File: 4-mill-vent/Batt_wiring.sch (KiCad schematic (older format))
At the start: 7 parts

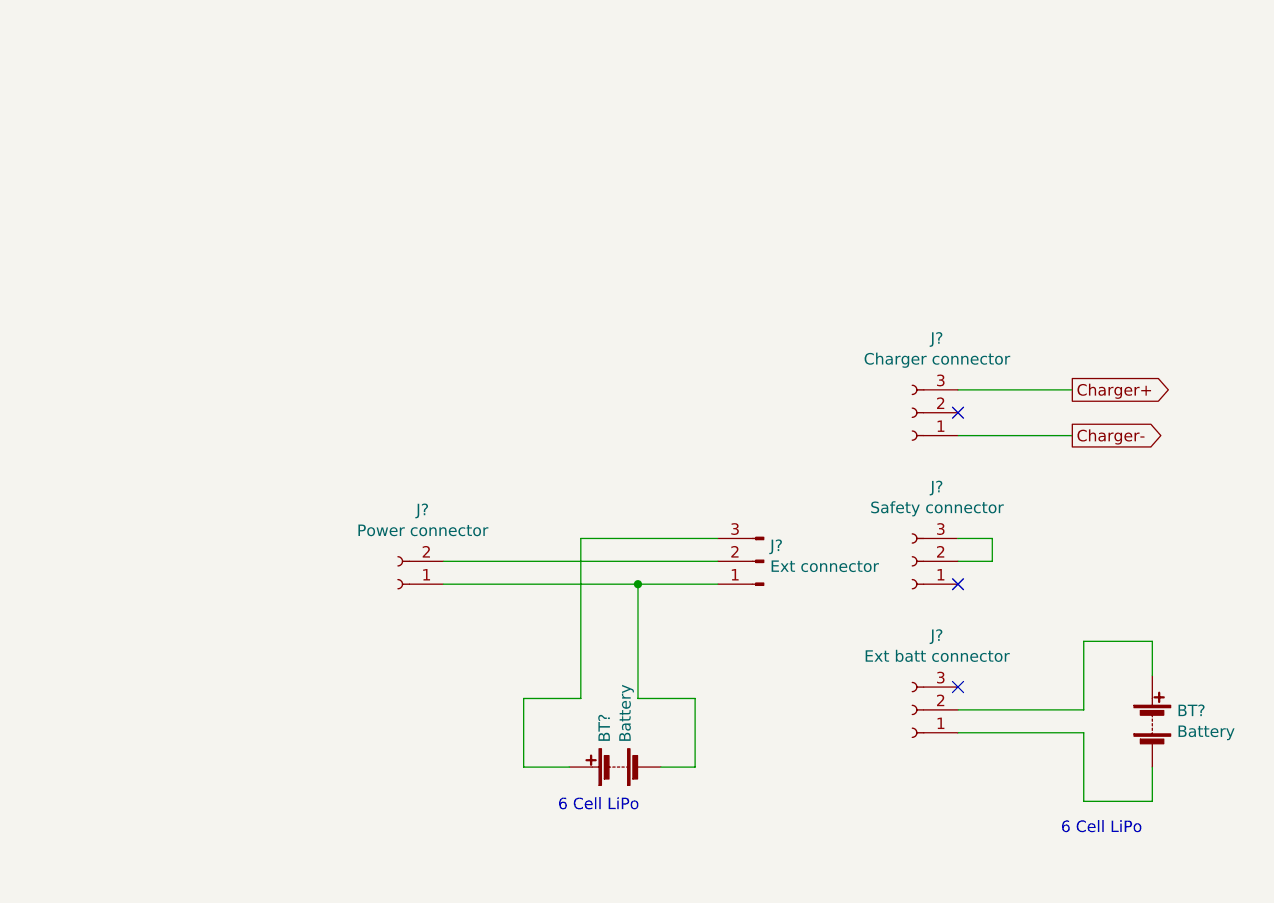
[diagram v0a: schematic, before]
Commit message: Added more to design
Had to add a transitor for allow the micro to power down the unit.
The reason is Q6's base can be as high as 16v when the on button is pressed.
This micro does not have open collector outputs and that would blow the chip.
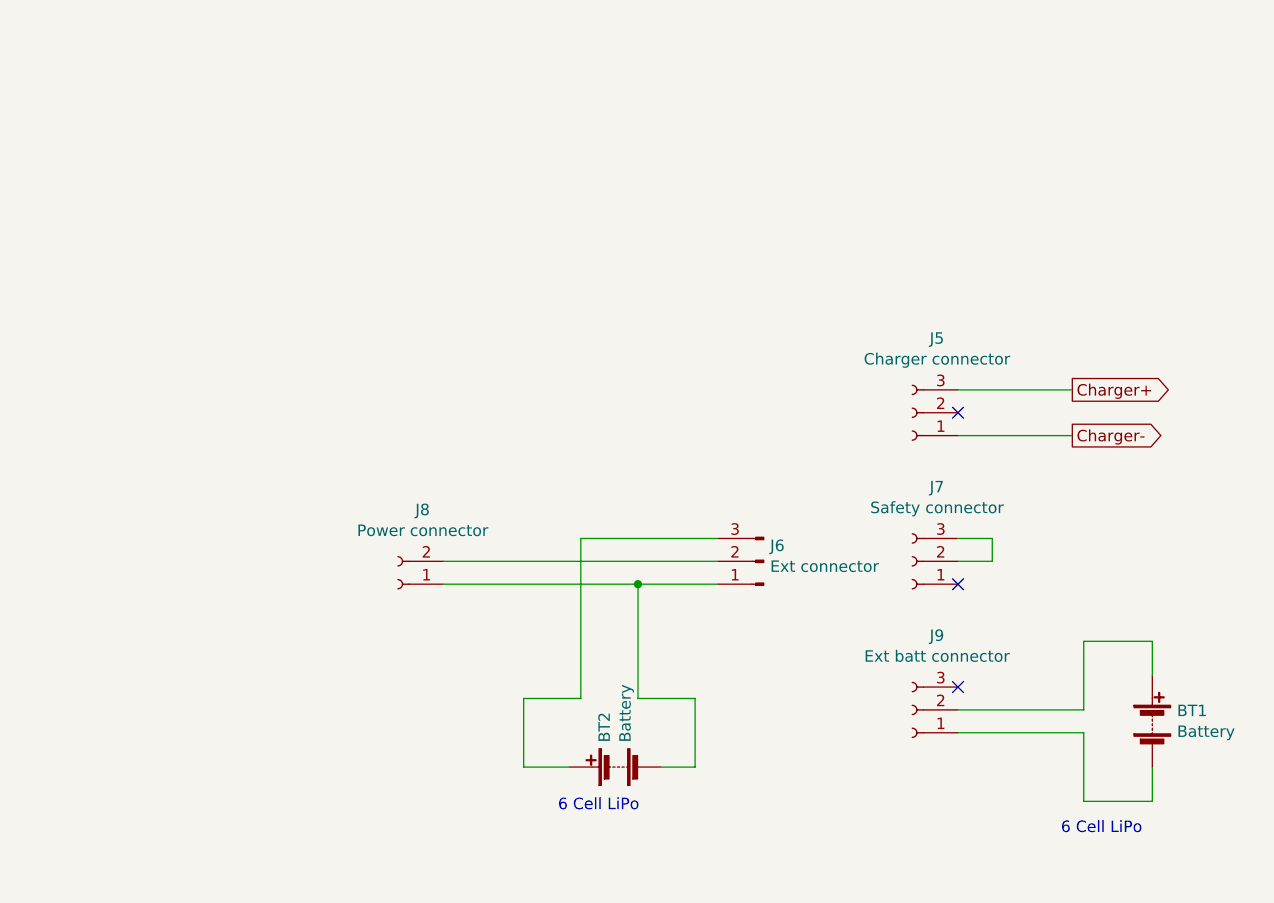
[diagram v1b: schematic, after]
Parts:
- gave numbers to parts that had none: 7
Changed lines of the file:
@@
 P 6250 3650
 AR Path="/5F8927BE" Ref="J?"  Part="1"
-AR Path="/5F88BDF3/5F8927BE" Ref="J?"  Part="1"
-F 0 "J?" H 6142 3325 50  0000 C CNN
+AR Path="/5F88BDF3/5F8927BE" Ref="J7"  Part="1"
+F 0 "J7" H 6142 3325 50  0000 C CNN
 F 1 "Safety connector" H 6142 3416 50  0000 C CNN
 F 2 "" H 6250 3650 50  0001 C CNN
@@
 P 6250 4300
 AR Path="/5F8927C4" Ref="J?"  Part="1"
-AR Path="/5F88BDF3/5F8927C4" Ref="J?"  Part="1"
-F 0 "J?" H 6142 3975 50  0000 C CNN
+AR Path="/5F88BDF3/5F8927C4" Ref="J9"  Part="1"
+F 0 "J9" H 6142 3975 50  0000 C CNN
 F 1 "Ext batt connector" H 6142 4066 50  0000 C CNN
 F 2 "" H 6250 4300 50  0001 C CNN
@@
 P 6250 3000
 AR Path="/5F8927CA" Ref="J?"  Part="1"
-AR Path="/5F88BDF3/5F8927CA" Ref="J?"  Part="1"
-F 0 "J?" H 6142 2675 50  0000 C CNN
+AR Path="/5F88BDF3/5F8927CA" Ref="J5"  Part="1"
+F 0 "J5" H 6142 2675 50  0000 C CNN
 F 1 "Charger connector" H 6142 2766 50  0000 C CNN
 F 2 "" H 6250 3000 50  0001 C CNN
@@
 P 5600 3650
 AR Path="/5F8927D0" Ref="J?"  Part="1"
-AR Path="/5F88BDF3/5F8927D0" Ref="J?"  Part="1"
-F 0 "J?" H 5572 3582 50  0000 R CNN
+AR Path="/5F88BDF3/5F8927D0" Ref="J6"  Part="1"
+F 0 "J6" H 5572 3582 50  0000 R CNN
 F 1 "Ext connector" H 5572 3673 50  0000 R CNN
 F 2 "" H 5600 3650 50  0001 C CNN
@@
 P 7300 4350
 AR Path="/5F8927DE" Ref="BT?"  Part="1"
-AR Path="/5F88BDF3/5F8927DE" Ref="BT?"  Part="1"
-F 0 "BT?" H 7408 4396 50  0000 L CNN
+AR Path="/5F88BDF3/5F8927DE" Ref="BT1"  Part="1"
+F 0 "BT1" H 7408 4396 50  0000 L CNN
 F 1 "Battery" H 7408 4305 50  0000 L CNN
 F 2 "" V 7300 4410 50  0001 C CNN
@@
 P 4950 4550
 AR Path="/5F8927E4" Ref="BT?"  Part="1"
-AR Path="/5F88BDF3/5F8927E4" Ref="BT?"  Part="1"
-F 0 "BT?" H 5058 4596 50  0000 L CNN
+AR Path="/5F88BDF3/5F8927E4" Ref="BT2"  Part="1"
+F 0 "BT2" H 5058 4596 50  0000 L CNN
 F 1 "Battery" H 5058 4505 50  0000 L CNN
 F 2 "" V 4950 4610 50  0001 C CNN
@@
 P 4000 3750
 AR Path="/5F8927FA" Ref="J?"  Part="1"
-AR Path="/5F88BDF3/5F8927FA" Ref="J?"  Part="1"
-F 0 "J?" H 3892 3425 50  0000 C CNN
+AR Path="/5F88BDF3/5F8927FA" Ref="J8"  Part="1"
+F 0 "J8" H 3892 3425 50  0000 C CNN
 F 1 "Power connector" H 3892 3516 50  0000 C CNN
 F 2 "" H 4000 3750 50  0001 C CNN

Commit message: BOM started
More updates to board
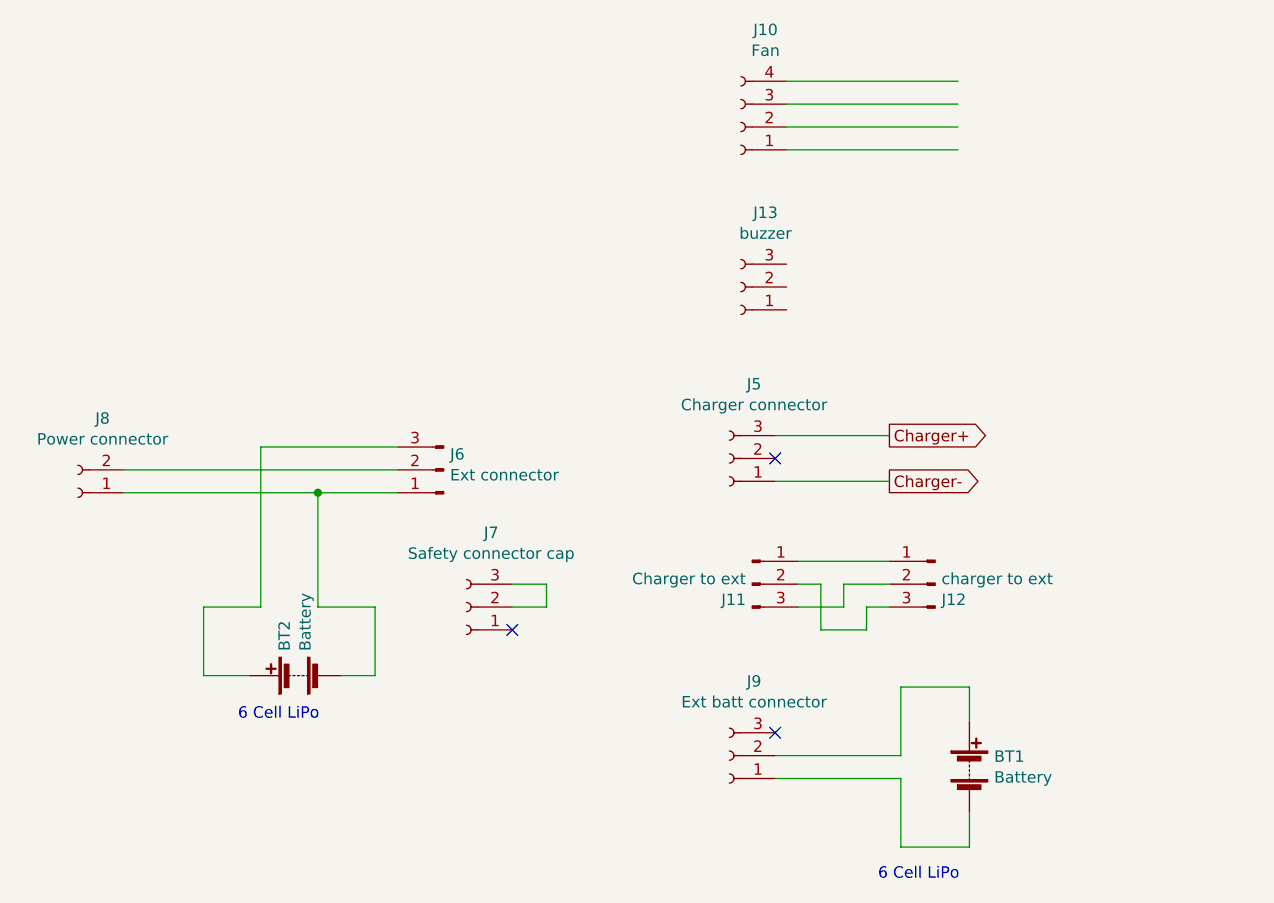
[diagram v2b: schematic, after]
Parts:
- added J10: Fan, symbol Connector:Conn_01x04_Female
- added J11: Charger to ext, symbol Connector:Conn_01x03_Male
- added J12: charger to ext, symbol Connector:Conn_01x03_Male
- added J13: buzzer, symbol Connector:Conn_01x03_Female
- J7: value Safety connector -> Safety connector cap
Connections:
- wire segments 25 -> 38
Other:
- moved on the sheet: BT1, BT2, J5, J6, J7, J8, J9
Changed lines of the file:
@@
 Comment4 ""
 $EndDescr
-Text GLabel 6950 2900 2    50   Output ~ 0
+Text GLabel 6150 3100 2    50   Output ~ 0
 Charger+
-Text GLabel 6950 3100 2    50   Output ~ 0
+Text GLabel 6150 3300 2    50   Output ~ 0
 Charger-
 Wire Wire Line
-	6450 3550 6600 3550
+	4500 3750 4650 3750
 $Comp
 L Connector:Conn_01x03_Female J?
 U 1 1 5F8927BE
-P 6250 3650
+P 4300 3850
 AR Path="/5F8927BE" Ref="J?"  Part="1"
 AR Path="/5F88BDF3/5F8927BE" Ref="J7"  Part="1"
-F 0 "J7" H 6142 3325 50  0000 C CNN
-F 1 "Safety connector" H 6142 3416 50  0000 C CNN
-F 2 "" H 6250 3650 50  0001 C CNN
-F 3 "~" H 6250 3650 50  0001 C CNN
-	1    6250 3650
+F 0 "J7" H 4192 3525 50  0000 C CNN
+F 1 "Safety connector cap" H 4192 3616 50  0000 C CNN
+F 2 "" H 4300 3850 50  0001 C CNN
+F 3 "~" H 4300 3850 50  0001 C CNN
+	1    4300 3850
 	-1   0    0    1
 $EndComp
@@
 L Connector:Conn_01x03_Female J?
 U 1 1 5F8927C4
-P 6250 4300
+P 5450 4500
 AR Path="/5F8927C4" Ref="J?"  Part="1"
 AR Path="/5F88BDF3/5F8927C4" Ref="J9"  Part="1"
-F 0 "J9" H 6142 3975 50  0000 C CNN
-F 1 "Ext batt connector" H 6142 4066 50  0000 C CNN
-F 2 "" H 6250 4300 50  0001 C CNN
-F 3 "~" H 6250 4300 50  0001 C CNN
-	1    6250 4300
+F 0 "J9" H 5342 4175 50  0000 C CNN
+F 1 "Ext batt connector" H 5342 4266 50  0000 C CNN
+F 2 "" H 5450 4500 50  0001 C CNN
+F 3 "~" H 5450 4500 50  0001 C CNN
+	1    5450 4500
 	-1   0    0    1
 $EndComp
@@
 L Connector:Conn_01x03_Female J?
 U 1 1 5F8927CA
-P 6250 3000
+P 5450 3200
 AR Path="/5F8927CA" Ref="J?"  Part="1"
 AR Path="/5F88BDF3/5F8927CA" Ref="J5"  Part="1"
-F 0 "J5" H 6142 2675 50  0000 C CNN
-F 1 "Charger connector" H 6142 2766 50  0000 C CNN
-F 2 "" H 6250 3000 50  0001 C CNN
-F 3 "~" H 6250 3000 50  0001 C CNN
-	1    6250 3000
+F 0 "J5" H 5342 2875 50  0000 C CNN
+F 1 "Charger connector" H 5342 2966 50  0000 C CNN
+F 2 "" H 5450 3200 50  0001 C CNN
+F 3 "~" H 5450 3200 50  0001 C CNN
+	1    5450 3200
 	-1   0    0    1
 $EndComp
@@
 L Connector:Conn_01x03_Male J?
 U 1 1 5F8927D0
-P 5600 3650
+P 4200 3250
 AR Path="/5F8927D0" Ref="J?"  Part="1"
 AR Path="/5F88BDF3/5F8927D0" Ref="J6"  Part="1"
-F 0 "J6" H 5572 3582 50  0000 R CNN
-F 1 "Ext connector" H 5572 3673 50  0000 R CNN
-F 2 "" H 5600 3650 50  0001 C CNN
-F 3 "~" H 5600 3650 50  0001 C CNN
-	1    5600 3650
-	-1   0    0    1
-$EndComp
-Wire Wire Line
-	6600 3550 6600 3650
-Wire Wire Line
-	6600 3650 6450 3650
-NoConn ~ 6450 3000
-NoConn ~ 6450 3750
-NoConn ~ 6450 4200
-Wire Wire Line
-	5400 3750 5050 3750
-Wire Wire Line
-	5050 3750 5050 4250
-Connection ~ 5050 3750
+F 0 "J6" H 4172 3182 50  0000 R CNN
+F 1 "Ext connector" H 4172 3273 50  0000 R CNN
+F 2 "" H 4200 3250 50  0001 C CNN
+F 3 "~" H 4200 3250 50  0001 C CNN
+	1    4200 3250
+	-1   0    0    1
+$EndComp
+Wire Wire Line
+	4650 3750 4650 3850
+Wire Wire Line
+	4650 3850 4500 3850
+NoConn ~ 5650 3200
+NoConn ~ 4500 3950
+NoConn ~ 5650 4400
+Wire Wire Line
+	4000 3350 3650 3350
+Wire Wire Line
+	3650 3350 3650 3850
+Connection ~ 3650 3350
 $Comp
 L Device:Battery BT?
 U 1 1 5F8927DE
-P 7300 4350
+P 6500 4550
 AR Path="/5F8927DE" Ref="BT?"  Part="1"
 AR Path="/5F88BDF3/5F8927DE" Ref="BT1"  Part="1"
-F 0 "BT1" H 7408 4396 50  0000 L CNN
-F 1 "Battery" H 7408 4305 50  0000 L CNN
-F 2 "" V 7300 4410 50  0001 C CNN
-F 3 "~" V 7300 4410 50  0001 C CNN
-	1    7300 4350
+F 0 "BT1" H 6608 4596 50  0000 L CNN
+F 1 "Battery" H 6608 4505 50  0000 L CNN
+F 2 "" V 6500 4610 50  0001 C CNN
+F 3 "~" V 6500 4610 50  0001 C CNN
+	1    6500 4550
 	1    0    0    -1
 $EndComp
@@
 L Device:Battery BT?
 U 1 1 5F8927E4
-P 4950 4550
+P 3550 4150
 AR Path="/5F8927E4" Ref="BT?"  Part="1"
 AR Path="/5F88BDF3/5F8927E4" Ref="BT2"  Part="1"
-F 0 "BT2" H 5058 4596 50  0000 L CNN
-F 1 "Battery" H 5058 4505 50  0000 L CNN
-F 2 "" V 4950 4610 50  0001 C CNN
-F 3 "~" V 4950 4610 50  0001 C CNN
-	1    4950 4550
+F 0 "BT2" H 3658 4196 50  0000 L CNN
+F 1 "Battery" H 3658 4105 50  0000 L CNN
+F 2 "" V 3550 4210 50  0001 C CNN
+F 3 "~" V 3550 4210 50  0001 C CNN
+	1    3550 4150
 	0    -1   -1   0
 $EndComp
 Wire Wire Line
-	7000 4300 7000 4000
-Wire Wire Line
-	7000 4000 7300 4000
-Wire Wire Line
-	7300 4000 7300 4150
-Wire Wire Line
-	7000 4400 7000 4700
-Wire Wire Line
-	7000 4700 7300 4700
-Wire Wire Line
-	7300 4700 7300 4550
-Wire Wire Line
-	5050 4250 5300 4250
-Wire Wire Line
-	5300 4250 5300 4550
-Wire Wire Line
-	5300 4550 5150 4550
-Wire Wire Line
-	4800 4250 4550 4250
-Wire Wire Line
-	4550 4250 4550 4550
-Wire Wire Line
-	4550 4550 4750 4550
-Wire Wire Line
-	6450 4300 7000 4300
-Wire Wire Line
-	6450 4400 7000 4400
-Wire Wire Line
-	6450 2900 6950 2900
-Wire Wire Line
-	6450 3100 6950 3100
+	6200 4500 6200 4200
+Wire Wire Line
+	6200 4200 6500 4200
+Wire Wire Line
+	6500 4200 6500 4350
+Wire Wire Line
+	6200 4600 6200 4900
+Wire Wire Line
+	6200 4900 6500 4900
+Wire Wire Line
+	6500 4900 6500 4750
+Wire Wire Line
+	3650 3850 3900 3850
+Wire Wire Line
+	3900 3850 3900 4150
+Wire Wire Line
+	3900 4150 3750 4150
+Wire Wire Line
+	3400 3850 3150 3850
+Wire Wire Line
+	3150 3850 3150 4150
+Wire Wire Line
+	3150 4150 3350 4150
+Wire Wire Line
+	5650 4500 6200 4500
+Wire Wire Line
+	5650 4600 6200 4600
+Wire Wire Line
+	5650 3100 6150 3100
+Wire Wire Line
+	5650 3300 6150 3300
 $Comp
 L Connector:Conn_01x02_Female J?
 U 1 1 5F8927FA
-P 4000 3750
+P 2600 3350
 AR Path="/5F8927FA" Ref="J?"  Part="1"
 AR Path="/5F88BDF3/5F8927FA" Ref="J8"  Part="1"
-F 0 "J8" H 3892 3425 50  0000 C CNN
-F 1 "Power connector" H 3892 3516 50  0000 C CNN
-F 2 "" H 4000 3750 50  0001 C CNN
-F 3 "~" H 4000 3750 50  0001 C CNN
-	1    4000 3750
-	-1   0    0    1
-$EndComp
-Wire Wire Line
-	4200 3750 5050 3750
-Wire Wire Line
-	4800 3550 5400 3550
-Wire Wire Line
-	4800 3550 4800 4250
-Wire Wire Line
-	4200 3650 5400 3650
-Text Notes 6900 4850 0    50   ~ 0
+F 0 "J8" H 2492 3025 50  0000 C CNN
+F 1 "Power connector" H 2492 3116 50  0000 C CNN
+F 2 "" H 2600 3350 50  0001 C CNN
+F 3 "~" H 2600 3350 50  0001 C CNN
+	1    2600 3350
+	-1   0    0    1
+$EndComp
+Wire Wire Line
+	2800 3350 3650 3350
+Wire Wire Line
+	3400 3150 4000 3150
+Wire Wire Line
+	3400 3150 3400 3850
+Wire Wire Line
+	2800 3250 4000 3250
+Text Notes 6100 5050 0    50   ~ 0
 6 Cell LiPo
-Text Notes 4700 4750 0    50   ~ 0
+Text Notes 3300 4350 0    50   ~ 0
 6 Cell LiPo
+$Comp
+L Connector:Conn_01x04_Female J10
+U 1 1 5F1C3804
+P 5500 1750
+F 0 "J10" H 5392 1325 50  0000 C CNN
+F 1 "Fan" H 5392 1416 50  0000 C CNN
+F 2 "" H 5500 1750 50  0001 C CNN
+F 3 "~" H 5500 1750 50  0001 C CNN
+	1    5500 1750
+	-1   0    0    1
+$EndComp
+Wire Wire Line
+	5700 1550 6450 1550
+Wire Wire Line
+	5700 1650 6450 1650
+Wire Wire Line
+	5700 1850 6450 1850
+Wire Wire Line
+	5700 1750 6450 1750
+$Comp
+L Connector:Conn_01x03_Male J?
+U 1 1 5F1CAFE0
+P 5550 3750
+AR Path="/5F1CAFE0" Ref="J?"  Part="1"
+AR Path="/5F88BDF3/5F1CAFE0" Ref="J11"  Part="1"
+F 0 "J11" H 5522 3682 50  0000 R CNN
+F 1 "Charger to ext" H 5522 3773 50  0000 R CNN
+F 2 "" H 5550 3750 50  0001 C CNN
+F 3 "~" H 5550 3750 50  0001 C CNN
+	1    5550 3750
+	1    0    0    -1
+$EndComp
+$Comp
+L Connector:Conn_01x03_Male J?
+U 1 1 5F1CC963
+P 6350 3750
+AR Path="/5F1CC963" Ref="J?"  Part="1"
+AR Path="/5F88BDF3/5F1CC963" Ref="J12"  Part="1"
+F 0 "J12" H 6322 3682 50  0000 R CNN
+F 1 "charger to ext" H 6322 3773 50  0000 R CNN
+F 2 "" H 6350 3750 50  0001 C CNN
+F 3 "~" H 6350 3750 50  0001 C CNN
+	1    6350 3750
+	-1   0    0    -1
+$EndComp
+Wire Wire Line
+	5950 3750 5950 3850
+Wire Wire Line
+	5950 3850 5750 3850
+Wire Wire Line
+	5750 3750 5850 3750
+Wire Wire Line
+	5850 3750 5850 3950
+Wire Wire Line
+	5850 3950 6050 3950
+Wire Wire Line
+	6150 3850 6050 3850
+Wire Wire Line
+	6050 3850 6050 3950
+Wire Wire Line
+	5950 3750 6150 3750
+Wire Wire Line
+	5750 3650 6150 3650
+$Comp
+L Connector:Conn_01x03_Female J?
+U 1 1 5F219686
+P 5500 2450
+AR Path="/5F219686" Ref="J?"  Part="1"
+AR Path="/5F88BDF3/5F219686" Ref="J13"  Part="1"
+F 0 "J13" H 5392 2125 50  0000 C CNN
+F 1 "buzzer" H 5392 2216 50  0000 C CNN
+F 2 "" H 5500 2450 50  0001 C CNN
+F 3 "~" H 5500 2450 50  0001 C CNN
+	1    5500 2450
+	-1   0    0    1
+$EndComp
 $EndSCHEMATC
